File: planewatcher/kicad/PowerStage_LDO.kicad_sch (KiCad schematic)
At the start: 11 parts, among them U6 LT3045IMSE-1#PBF

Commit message: added lcsc_ids to all parts
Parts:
- C19, C21: lcsc_id (none) -> C3903725
- C22: lcsc_id (none) -> C161163
- C26: lcsc_id (none) -> C913474
- C27: lcsc_id (none) -> C3883047
- L5: lcsc_id (none) -> C41556732
- R18: lcsc_id (none) -> C191915
- R19: lcsc_id (none) -> C2088292
- R22: lcsc_id (none) -> C4054572
- U6: lcsc_id (none) -> C666588
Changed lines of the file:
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@@
+			)
+		)
+		(property "lcsc_id" "C41556732"
+			(at 128.27 66.04 0)
+			(hide yes)
+			(show_name no)
+			(do_not_autoplace no)
+			(effects
+				(font
+					(size 1.27 1.27)
+				)
 			)
 		)
@@
 			)
 		)
+		(property "lcsc_id" "C3903725"
+			(at 138.43 69.85 0)
+			(hide yes)
+			(show_name no)
+			(do_not_autoplace no)
+			(effects
+				(font
+					(size 1.27 1.27)
+				)
+			)
+		)
 		(pin "1"
 		)
@@
 			)
 		)
+		(property "lcsc_id" "C3883047"
+			(at 234.95 81.28 0)
+			(hide yes)
+			(show_name no)
+			(do_not_autoplace no)
+			(effects
+				(font
+					(size 1.27 1.27)
+				)
+			)
+		)
 		(pin "1"
 		)
@@
 			)
 		)
+		(property "lcsc_id" "C4054572"
+			(at 190.5 102.87 0)
+			(hide yes)
+			(show_name no)
+			(do_not_autoplace no)
+			(effects
+				(font
+					(size 1.27 1.27)
+				)
+			)
+		)
 		(pin "1"
 		)
@@
 			)
 		)
+		(property "lcsc_id" "C191915"
+			(at 180.34 49.53 0)
+			(hide yes)
+			(show_name no)
+			(do_not_autoplace no)
+			(effects
+				(font
+					(size 1.27 1.27)
+				)
+			)
+		)
 		(pin "2"
 		)
@@
 			)
 		)
+		(property "lcsc_id" "C666588"
+			(at 207.01 58.42 0)
+			(hide yes)
+			(show_name no)
+			(do_not_autoplace no)
+			(effects
+				(font
+					(size 1.27 1.27)
+				)
+			)
+		)
 		(pin "2"
 		)
@@
 			)
 		)
+		(property "lcsc_id" "C3903725"
+			(at 118.11 69.85 0)
+			(hide yes)
+			(show_name no)
+			(do_not_autoplace no)
+			(effects
+				(font
+					(size 1.27 1.27)
+				)
+			)
+		)
 		(pin "1"
 		)
@@
 			)
 		)
+		(property "lcsc_id" "C913474"
+			(at 177.8 102.87 0)
+			(hide yes)
+			(show_name no)
+			(do_not_autoplace no)
+			(effects
+				(font
+					(size 1.27 1.27)
+				)
+			)
+		)
 		(property "Manufacturer" "Murata Electronics"
 			(at 177.8 102.87 0)
@@
 			)
 		)
+		(property "lcsc_id" "C161163"
+			(at 158.75 69.85 0)
+			(hide yes)
+			(show_name no)
+			(do_not_autoplace no)
+			(effects
+				(font
+					(size 1.27 1.27)
+				)
+			)
+		)
 		(pin "1"
 		)
@@
 			(hide yes)
 			(show_name no)
+			(do_not_autoplace no)
+			(effects
+				(font
+					(size 1.27 1.27)
+				)
+			)
+		)
+		(property "lcsc_id" "C2088292"
+			(at 190.5 49.53 0)
+			(hide yes)
+			(show_name no)

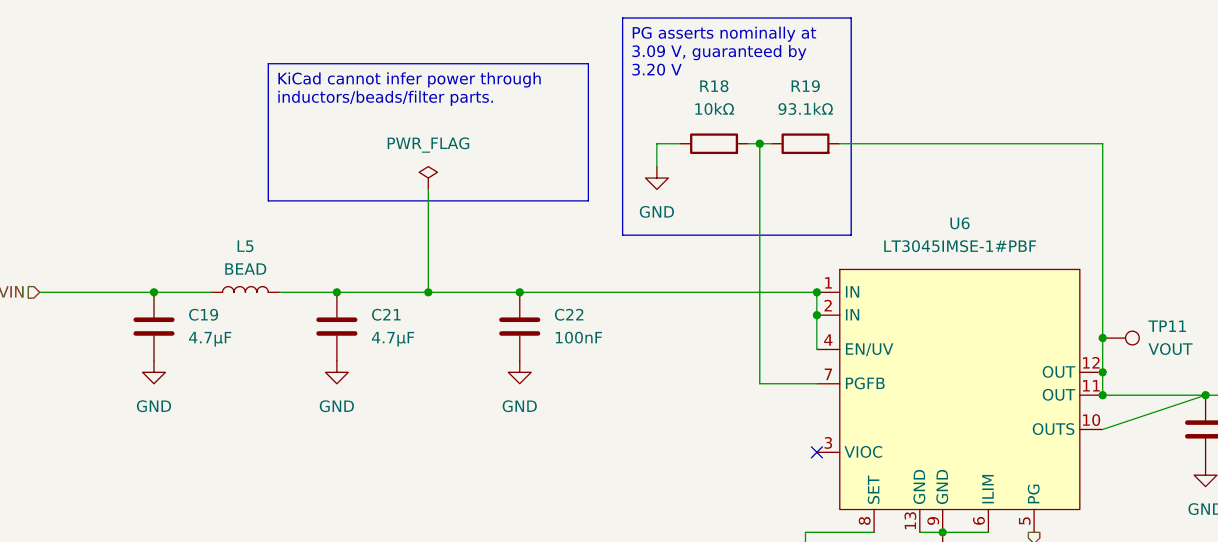
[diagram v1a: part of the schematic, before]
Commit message: update BoM to available parts from LCSC
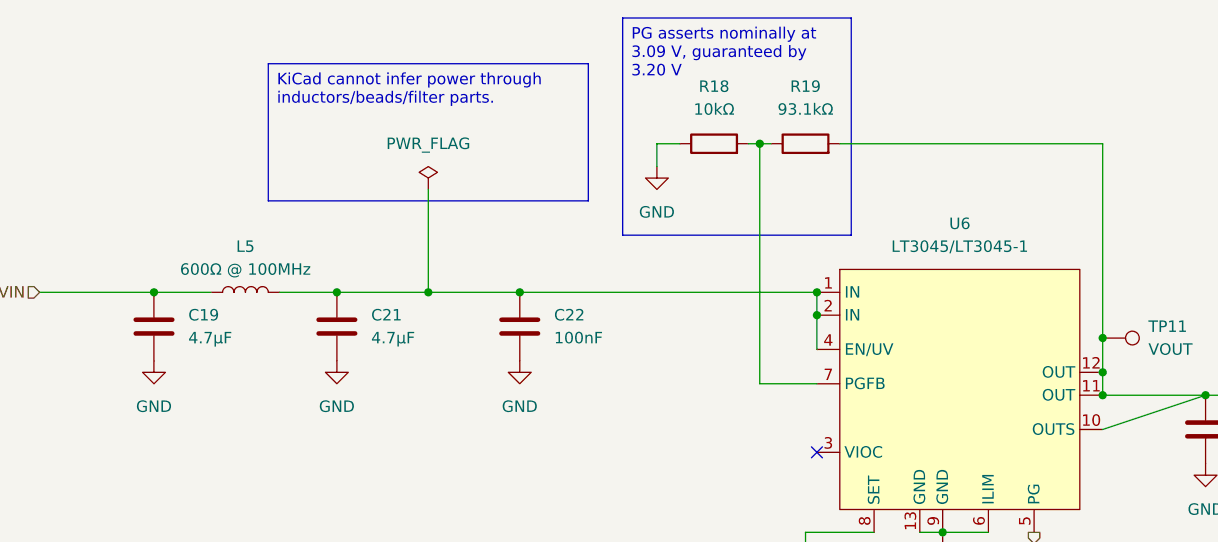
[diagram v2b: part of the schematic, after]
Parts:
- C19, C21: MPN GCJ31CR71C475KA01L -> CL31B475KBHNNNE; Manufacturer Murata Electronics -> Samsung Electro-Mechanics; lcsc_id C3903725 -> C51205
- C27: MPN GCJ31CR71A226KE01K -> CL31B226KPHNNNE; Manufacturer Murata Electronics -> Samsung Electro-Mechanics; lcsc_id C3883047 -> C87996
- L5: value BEAD -> 600Ω @ 100MHz; MPN BLM21PG601SN1D -> BLM21SP601SN1D; Manufacturer Murata -> muRata BLM21SP601SN1D; lcsc_id C41556732 -> C3716677
- R19: MPN ERA-2AEB9312X -> TNPW040293K1BEED; Manufacturer Panasonic Industry -> VISHAY; lcsc_id C2088292 -> C2088785
- R22: MPN ERA-3ARB3322V -> RT0603BRB0733K2L; Manufacturer Panasonic Industry -> YAGEO; lcsc_id C4054572 -> C860335
- U6: value LT3045IMSE-1#PBF -> LT3045/LT3045-1; MPN LT3045IMSE-1#PBF -> LT3045IMSE#TRPBF; lcsc_id C666588 -> C666587
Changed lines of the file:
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@@
 			)
 		)
-		(property "Value" "BEAD"
+		(property "Value" "600Ω @ 100MHz"
 			(at 128.27 63.5 90)
 			(show_name no)
@@
 			)
 		)
-		(property "MPN" "BLM21PG601SN1D"
+		(property "MPN" "BLM21SP601SN1D"
 			(at 128.27 66.04 0)
 			(hide yes)
@@
 			)
 		)
-		(property "Manufacturer" "Murata"
+		(property "Manufacturer" "muRata BLM21SP601SN1D"
 			(at 128.27 66.04 0)
 			(hide yes)
@@
 			)
 		)
-		(property "lcsc_id" "C41556732"
+		(property "lcsc_id" "C3716677"
 			(at 128.27 66.04 0)
 			(hide yes)
@@
 			)
 		)
-		(property "MPN" "GCJ31CR71C475KA01L"
+		(property "MPN" "CL31B475KBHNNNE"
 			(at 138.43 69.85 0)
 			(hide yes)
@@
 			)
 		)
-		(property "Manufacturer" "Murata Electronics"
+		(property "Manufacturer" "Samsung Electro-Mechanics"
 			(at 138.43 69.85 0)
 			(hide yes)
@@
 			)
 		)
-		(property "lcsc_id" "C3903725"
+		(property "lcsc_id" "C51205"
 			(at 138.43 69.85 0)
 			(hide yes)
@@
 			)
 		)
-		(property "MPN" "GCJ31CR71A226KE01K"
+		(property "MPN" "CL31B226KPHNNNE"
 			(at 234.95 81.28 0)
 			(hide yes)
@@
 			)
 		)
-		(property "Manufacturer" "Murata Electronics"
+		(property "Manufacturer" "Samsung Electro-Mechanics"
 			(at 234.95 81.28 0)
 			(hide yes)
@@
 			)
 		)
-		(property "lcsc_id" "C3883047"
+		(property "lcsc_id" "C87996"
 			(at 234.95 81.28 0)
 			(hide yes)
@@
 			)
 		)
-		(property "Description" "33.2 kOhms ±0.1% 0.1W, 1/10W Chip Resistor 0603 (1608 Metric) Automotive AEC-Q200 Thin Film"
+		(property "Description" "100mW 33.2kΩ Thin Film Resistor ±0.1% ±10ppm/℃ 0603 Chip Resistor - Surface Mount RoHS"
 			(at 190.5 102.87 0)
 			(hide yes)
@@
 			)
 		)
-		(property "MPN" "ERA-3ARB3322V"
+		(property "MPN" "RT0603BRB0733K2L"
 			(at 190.5 102.87 0)
 			(hide yes)
@@
 			)
 		)
-		(property "Manufacturer" "Panasonic Industry"
+		(property "Manufacturer" "YAGEO"
 			(at 190.5 102.87 0)
 			(hide yes)
@@
 			)
 		)
-		(property "lcsc_id" "C4054572"
+		(property "lcsc_id" "C860335"
 			(at 190.5 102.87 0)
 			(hide yes)
@@
 			)
 		)
-		(property "Value" "LT3045IMSE-1#PBF"
+		(property "Value" "LT3045/LT3045-1"
 			(at 207.645 60.96 0)
 			(show_name no)
@@
 			)
 		)
-		(property "MPN" "LT3045IMSE-1#PBF"
+		(property "MPN" "LT3045IMSE#TRPBF"
 			(at 207.01 58.42 0)
 			(hide yes)
@@
 			)
 		)
-		(property "lcsc_id" "C666588"
+		(property "lcsc_id" "C666587"
 			(at 207.01 58.42 0)
 			(hide yes)
@@
 			)
 		)
-		(property "MPN" "GCJ31CR71C475KA01L"
+		(property "MPN" "CL31B475KBHNNNE"
 			(at 118.11 69.85 0)
 			(hide yes)
@@
 			)
 		)
-		(property "Manufacturer" "Murata Electronics"
+		(property "Manufacturer" "Samsung Electro-Mechanics"
 			(at 118.11 69.85 0)
 			(hide yes)
@@
 			)
 		)
-		(property "lcsc_id" "C3903725"
+		(property "lcsc_id" "C51205"
 			(at 118.11 69.85 0)
 			(hide yes)
@@
 			)
 		)
-		(property "Description" "93.1 kOhms ±0.1% 0.063W, 1/16W Chip Resistor 0402 (1005 Metric) Automotive AEC-Q200 Thin Film"
+		(property "Description" "100mW 93.1kΩ 50V Thin Film Resistor ±0.1% ±25ppm/℃ 0402 Chip Resistor - Surface Mount RoHS"
 			(at 190.5 49.53 0)
 			(hide yes)
@@
 			)
 		)
-		(property "MPN" "ERA-2AEB9312X"
+		(property "MPN" "TNPW040293K1BEED"
 			(at 190.5 49.53 0)
 			(hide yes)
@@
 			)
 		)
-		(property "Manufacturer" "Panasonic Industry"
+		(property "Manufacturer" "VISHAY"
 			(at 190.5 49.53 0)
 			(hide yes)
@@
 			)
 		)
-		(property "lcsc_id" "C2088292"
+		(property "lcsc_id" "C2088785"
 			(at 190.5 49.53 0)
 			(hide yes)

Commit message: Change all test point footprints to TestPoint_THTPad_D1.0mm_Drill0.5mm
Had to move TP15 slightly to prevent it shorting to 3V3.
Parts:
- TP11: footprint TestPoint:TestPoint_Pad_D1.0mm -> TestPoint:TestPoint_THTPad_D1.0mm_Drill0.5mm
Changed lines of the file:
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@@
 			)
 		)
-		(property "Footprint" "TestPoint:TestPoint_Pad_D1.0mm"
+		(property "Footprint" "TestPoint:TestPoint_THTPad_D1.0mm_Drill0.5mm"
 			(at 223.52 76.2 0)
 			(hide yes)

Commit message: Update purpose fields with more descriptive text for future me
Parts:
- C21: Purpose Low freq bypass capacitor for the LT3045-1. -> Low-frequency bulk bypass capacitor on the filtered LT3045 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
- C22: Purpose High freq bypass capacitor for the LT3045-1. -> High-frequency bypass capacitor on the filtered LT3045 inpu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
- L5: Purpose Filters high-frequency switching noise on the low-noise reg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 -> Ferrite bead input filter feeding the LT3045 IN/EN node fro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
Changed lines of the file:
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@@
 			)
 		)
-		(property "Purpose" "Filters high-frequency switching noise on the low-noise regulator rail."
+		(property "Purpose" "Ferrite bead input filter feeding the LT3045 IN/EN node from 4V5; attenuates high-frequency switching noise before the low-noise regulator."
 			(at 128.27 66.04 0)
 			(hide yes)
@@
 			)
 		)
-		(property "Purpose" "Low freq bypass capacitor for the LT3045-1."
+		(property "Purpose" "Low-frequency bulk bypass capacitor on the filtered LT3045 input/EN node."
 			(at 138.43 69.85 0)
 			(hide yes)
@@
 			)
 		)
-		(property "Purpose" "High freq bypass capacitor for the LT3045-1."
+		(property "Purpose" "High-frequency bypass capacitor on the filtered LT3045 input/EN node."
 			(at 158.75 69.85 0)
 			(hide yes)
